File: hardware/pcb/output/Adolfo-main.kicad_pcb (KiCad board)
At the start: 2 copper layers, 96.2 x 110.5 mm, 156 parts, among them U1 Daisy Seed 3 / Seed2 DFM comp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, U10 OPA4197ID candidate, U11 OPA4197ID candidate, U12 SN74AHCT125 candidate, U13 SN74AHCT125 candidate, U2 AD7606C-18 candidate, U3 DAC8568B (gain 1, midscale re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, U4 MCP23017-E/SO candidate, U5 SN74LVC08A candidate, U6 SN74LVC08A candidate, U7 ADG5412FBRUZ candidate, U8 ADG5412FBRUZ candidate, U9 OPA4197ID candidate

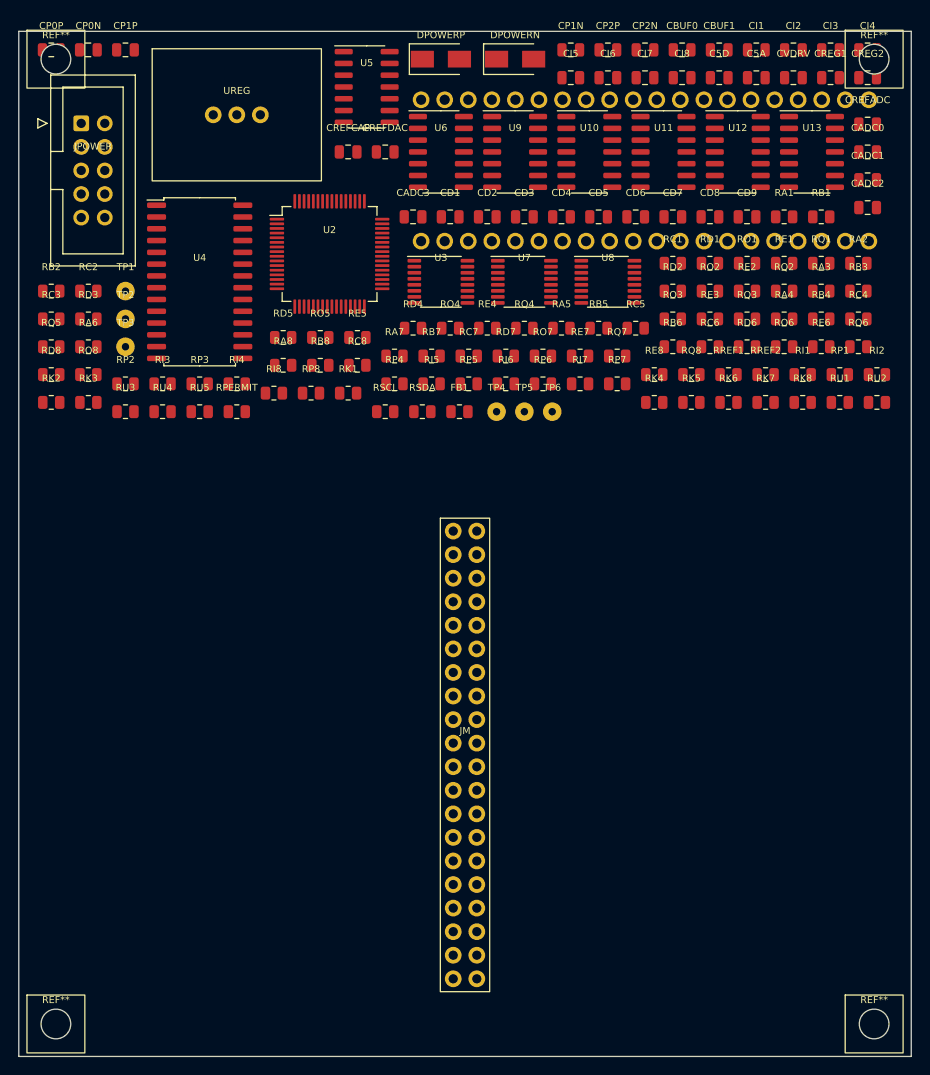
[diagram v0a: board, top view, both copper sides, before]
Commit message: fix(pcb): harden 20hp carrier and center panel display
Complete rev D schematics, routed boards and native KiCad checks.
Fix input normals, reset latch, fault resistor ratings and via placement.
Center the OLED module and window; update routing and mechanical exports.
Record supply sequencing, 5 V supervision and converter backend blockers.

Validation: 2027 CAD checks, zero ERC/DRC violations, host and SPICE tests.
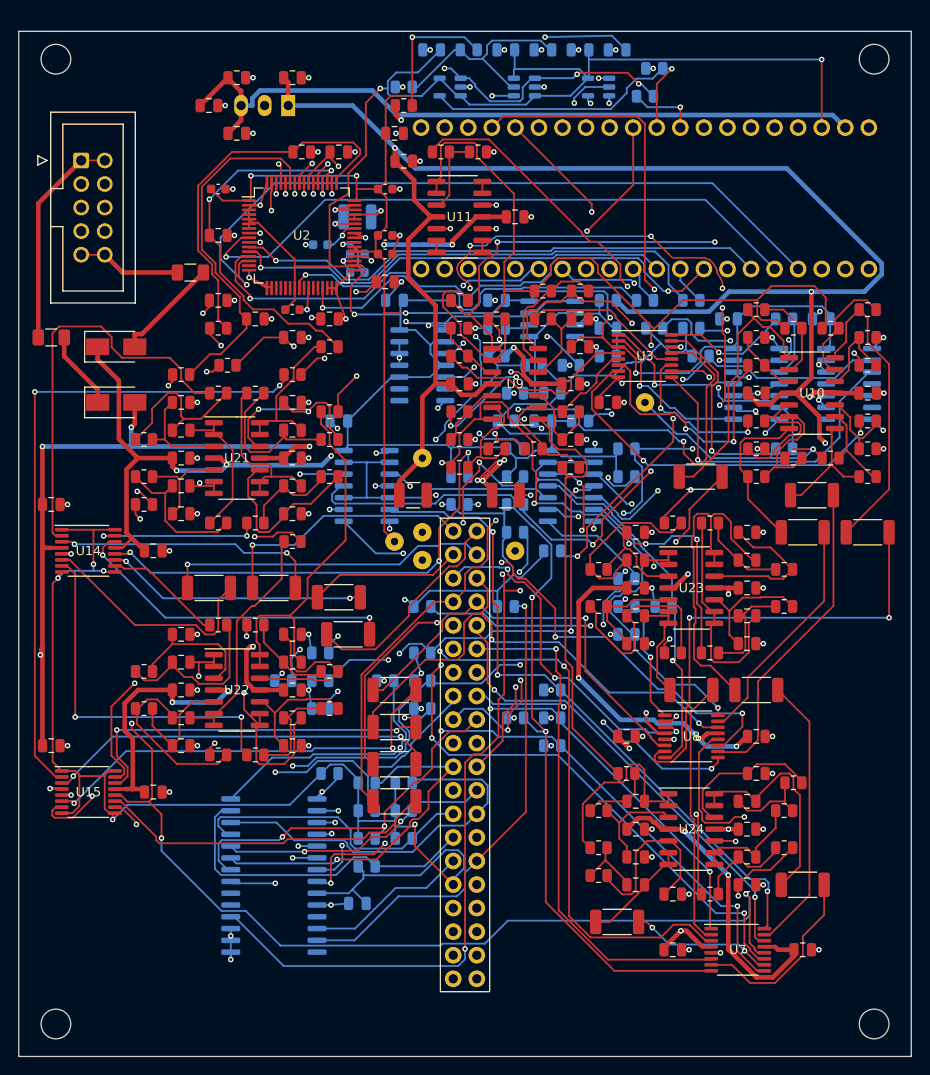
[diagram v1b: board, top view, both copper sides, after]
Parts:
- removed C5A: 10uF 10V, ADOLFO:c0805
- removed C5D: 47uF 10V, ADOLFO:c0805
- removed CP0N, CP0P, CP1N, CP1P, CP2N, CP2P: 100nF 50V, ADOLFO:c0805
- removed CREFADC, CREFDAC, CVDRV: 100nF, ADOLFO:c0805
- removed CREFCAP: 10uF low ESR, ADOLFO:c0805
- removed DPOWERN, DPOWERP: SS14, ADOLFO:sma
- removed JM: Panel link 2x20 candidate, ADOLFO:header40
- removed JPOWER: Eurorack IDC10 keyed, ADOLFO:idc10
- removed RPERMIT: 10k, ADOLFO:r0805
- removed RSCL, RSDA: 4.7k DNP, ADOLFO:r0805
- removed UREG: 5V >=1A module - selection OPEN, ADOLFO:power_module
- added C1: 100nF 50V, ADOLFO:c0805, F.Cu at (50.0, 47.0)
- added C10: 100nF, ADOLFO:c0603, B.Cu at (35.0, 32.0)
- added C11: 10uF 25V X7R low ESR, ADOLFO:c1210, B.Cu at (39.0, 29.0)
- added C12: 100nF, ADOLFO:c0805, F.Cu at (66.0, 49.0)
- added C13: 10nF, ADOLFO:c0805, B.Cu at (66.0, 41.0)
- added C14: 1nF, ADOLFO:c0805, B.Cu at (54.0, 41.0)
- added C15: 10nF, ADOLFO:c0805, B.Cu at (67.0, 11.0)
- added C16: 100nF 50V, ADOLFO:c0805, F.Cu at (17.0, 65.0)
- added C17: 100nF 50V, ADOLFO:c0805, F.Cu at (6.00, 60.0)
- added C18: 100nF 50V, ADOLFO:c0805, F.Cu at (17.0, 91.0)
- added C19: 100nF 50V, ADOLFO:c0805, F.Cu at (6.00, 86.0)
- added C2: 100nF 50V, ADOLFO:c0805, F.Cu at (62.0, 47.0)
- added C20: 820pF C0G 1%, ADOLFO:c0805, F.Cu at (20.0, 52.0)
- added C21: 680pF C0G 1%, ADOLFO:c0805, F.Cu at (20.0, 49.0)
- added C22: 1.8nF C0G 1%, ADOLFO:c0805, F.Cu at (20.0, 58.0)
- added C23: 270pF C0G 1%, ADOLFO:c0805, F.Cu at (20.0, 61.0)
- added C24: 820pF C0G 1%, ADOLFO:c0805, F.Cu at (32.0, 58.0)
- added C25: 680pF C0G 1%, ADOLFO:c0805, F.Cu at (32.0, 61.0)
- added C26: 1.8nF C0G 1%, ADOLFO:c0805, F.Cu at (32.0, 52.0)
- added C27: 270pF C0G 1%, ADOLFO:c0805, F.Cu at (32.0, 49.0)
- added C28: 820pF C0G 1%, ADOLFO:c0805, F.Cu at (20.0, 77.0)
- added C29: 680pF C0G 1%, ADOLFO:c0805, F.Cu at (20.0, 74.0)
- added C3: 100nF 50V, ADOLFO:c0805, F.Cu at (82.0, 48.0)
- added C30: 1.8nF C0G 1%, ADOLFO:c0805, F.Cu at (20.0, 83.0)
- added C31: 270pF C0G 1%, ADOLFO:c0805, F.Cu at (20.0, 86.0)
- added C32: 820pF C0G 1%, ADOLFO:c0805, F.Cu at (32.0, 83.0)
- added C33: 680pF C0G 1%, ADOLFO:c0805, F.Cu at (32.0, 86.0)
- added C34: 1.8nF C0G 1%, ADOLFO:c0805, F.Cu at (32.0, 77.0)
- added C35: 270pF C0G 1%, ADOLFO:c0805, F.Cu at (32.0, 74.0)
- added C36: 820pF C0G 1%, ADOLFO:c0805, F.Cu at (69.0, 66.0)
- added C37: 680pF C0G 1%, ADOLFO:c0805, F.Cu at (69.0, 63.0)
- added C38: 1.8nF C0G 1%, ADOLFO:c0805, F.Cu at (69.0, 72.0)
- added C39: 270pF C0G 1%, ADOLFO:c0805, F.Cu at (69.0, 75.0)
- added C4: 100nF 50V, ADOLFO:c0805, F.Cu at (94.0, 48.0)
- added C40: 820pF C0G 1%, ADOLFO:c0805, F.Cu at (81.0, 72.0)
- added C41: 680pF C0G 1%, ADOLFO:c0805, F.Cu at (81.0, 75.0)
- added C42: 1.8nF C0G 1%, ADOLFO:c0805, F.Cu at (81.0, 66.0)
- added C43: 270pF C0G 1%, ADOLFO:c0805, F.Cu at (81.0, 63.0)
- added C44: 820pF C0G 1%, ADOLFO:c0805, F.Cu at (69.0, 92.0)
- added C45: 680pF C0G 1%, ADOLFO:c0805, F.Cu at (69.0, 98.0)
- added C46: 1.8nF C0G 1%, ADOLFO:c0805, F.Cu at (69.0, 101.0)
- added C47: 270pF C0G 1%, ADOLFO:c0805, F.Cu at (73.0, 102.0)
- added C48: 820pF C0G 1%, ADOLFO:c0805, F.Cu at (81.0, 98.0)
- added C49: 680pF C0G 1%, ADOLFO:c0805, F.Cu at (81.0, 101.0)
- added C5: 100nF 50V, ADOLFO:c0805, F.Cu at (44.0, 23.0)
- added C50: 1.8nF C0G 1%, ADOLFO:c0805, F.Cu at (81.0, 92.0)
- added C51: 270pF C0G 1%, ADOLFO:c0805, F.Cu at (82.0, 89.0)
- added C52: 100nF 50V, ADOLFO:c0805, F.Cu at (20.0, 55.0)
- added C53: 100nF 50V, ADOLFO:c0805, F.Cu at (32.0, 55.0)
- added C54: 100nF 50V, ADOLFO:c0805, F.Cu at (20.0, 80.0)
- added C55: 100nF 50V, ADOLFO:c0805, F.Cu at (32.0, 80.0)
- added C56: 100nF 50V, ADOLFO:c0805, F.Cu at (69.0, 69.0)
- added C57: 100nF 50V, ADOLFO:c0805, F.Cu at (81.0, 69.0)
- added C58: 100nF 50V, ADOLFO:c0805, F.Cu at (69.0, 95.0)
- added C59: 100nF 50V, ADOLFO:c0805, F.Cu at (81.0, 95.0)
- added C6: 100nF 50V, ADOLFO:c0805, F.Cu at (56.0, 29.0)
- added C60: 22uF 25V X7R, ADOLFO:c1210, F.Cu at (45.0, 59.0)
- added C61: 22uF 25V X7R, ADOLFO:c1210, F.Cu at (55.0, 59.0)
- added C62: 100nF 50V, ADOLFO:c0805, F.Cu at (32.0, 14.0)
- added C63: 100nF, ADOLFO:c0805, F.Cu at (23.0, 17.0)
- added C7: 47uF 10V, ADOLFO:c0805, F.Cu at (26.0, 14.0)
- added C8: 10uF 10V, ADOLFO:c0805, F.Cu at (43.0, 20.0)
- added C9: 100nF, ADOLFO:c0603, F.Cu at (32.0, 39.0)
- added CMON5: 10nF, ADOLFO:c0805, B.Cu at (59.0, 11.0)
- added CSAFE16: 100nF, ADOLFO:c0805, B.Cu at (43.0, 38.0)
- added CSAFE17: 100nF, ADOLFO:c0805, B.Cu at (47.0, 11.0)
- added CSAFE18: 100nF, ADOLFO:c0805, B.Cu at (55.0, 11.0)
- added CSAFE19: 100nF, ADOLFO:c0805, B.Cu at (54.0, 38.0)
- added CSAFE20: 100nF, ADOLFO:c0805, B.Cu at (63.0, 11.0)
- added D1: SS14, ADOLFO:sma, F.Cu at (13.0, 43.0)
- added D2: SS14, ADOLFO:sma, F.Cu at (13.0, 49.0)
- added D3: BAT54WS, ADOLFO:sod323, B.Cu at (52.0, 47.0)
- added F1: Littelfuse 1206L075/24YR, ADOLFO:fuse1206, F.Cu at (21.0, 35.0)
- added F2: Littelfuse 1206L025/30YR, ADOLFO:fuse1206, F.Cu at (6.00, 42.0)
- added J13: Samtec TSW-120-07-G-D, ADOLFO:header40, F.Cu at (50.6, 87.0)
- added J16: Wurth 61201021621 IDC10, ADOLFO:idc10, F.Cu at (10.5, 28.0)
- added R1: 10k, ADOLFO:r0805, B.Cu at (62.0, 45.0)
- added R10: 11k 0.1%, ADOLFO:r0805, F.Cu at (16.0, 53.0)
- added R11: 11k 0.1%, ADOLFO:r0805, F.Cu at (24.0, 62.0)
- added R12: 11k 0.1%, ADOLFO:r0805, F.Cu at (16.0, 57.0)
- added R13: 11k 0.1%, ADOLFO:r0805, F.Cu at (28.0, 62.0)
- added R14: 11k 0.1%, ADOLFO:r0805, F.Cu at (36.0, 57.0)
- added R15: 11k 0.1%, ADOLFO:r0805, F.Cu at (28.0, 48.0)
- added R16: 11k 0.1%, ADOLFO:r0805, F.Cu at (36.0, 53.0)
- added R17: 11k 0.1%, ADOLFO:r0805, F.Cu at (24.0, 73.0)
- added R18: 11k 0.1%, ADOLFO:r0805, F.Cu at (16.0, 78.0)
- added R19: 11k 0.1%, ADOLFO:r0805, F.Cu at (24.0, 87.0)
- added R2: 2.2k, ADOLFO:r0805, B.Cu at (46.0, 71.0)
- added R20: 11k 0.1%, ADOLFO:r0805, F.Cu at (16.0, 82.0)
- added R21: 11k 0.1%, ADOLFO:r0805, F.Cu at (28.0, 87.0)
- added R22: 11k 0.1%, ADOLFO:r0805, F.Cu at (36.0, 82.0)
- added R23: 11k 0.1%, ADOLFO:r0805, F.Cu at (28.0, 73.0)
- added R24: 11k 0.1%, ADOLFO:r0805, F.Cu at (36.0, 78.0)
- added R25: 11k 0.1%, ADOLFO:r0805, F.Cu at (73.0, 62.0)
- added R26: 11k 0.1%, ADOLFO:r0805, F.Cu at (65.0, 67.0)
- added R27: 11k 0.1%, ADOLFO:r0805, F.Cu at (73.0, 76.0)
- added R28: 11k 0.1%, ADOLFO:r0805, F.Cu at (65.0, 71.0)
- added R29: 11k 0.1%, ADOLFO:r0805, F.Cu at (77.0, 76.0)
- added R3: 2.2k, ADOLFO:r0805, B.Cu at (55.0, 71.0)
- added R30: 11k 0.1%, ADOLFO:r0805, F.Cu at (85.0, 71.0)
- added R31: 11k 0.1%, ADOLFO:r0805, F.Cu at (77.0, 62.0)
- added R32: 11k 0.1%, ADOLFO:r0805, F.Cu at (85.0, 67.0)
- added R33: 11k 0.1%, ADOLFO:r0805, F.Cu at (68.0, 89.0)
- added R34: 11k 0.1%, ADOLFO:r0805, F.Cu at (65.0, 93.0)
- added R35: 11k 0.1%, ADOLFO:r0805, F.Cu at (65.0, 97.0)
- added R36: 11k 0.1%, ADOLFO:r0805, F.Cu at (65.0, 100.0)
- added R37: 11k 0.1%, ADOLFO:r0805, F.Cu at (77.0, 102.0)
- added R38: 11k 0.1%, ADOLFO:r0805, F.Cu at (85.0, 97.0)
- added R39: 11k 0.1%, ADOLFO:r0805, F.Cu at (85.0, 93.0)
- added R4: 0R, ADOLFO:r0805, B.Cu at (70.0, 16.0)
- added R40: 11k 0.1%, ADOLFO:r0805, F.Cu at (86.0, 90.0)
- added R41: 10k, ADOLFO:r0805, B.Cu at (68.0, 54.0)
- added R42: 33R, ADOLFO:r0805, B.Cu at (75.0, 38.0)
- added R43: 33R, ADOLFO:r0805, B.Cu at (70.0, 38.0)
- added R44: 33R, ADOLFO:r0805, B.Cu at (85.0, 40.0)
- added R45: 33R, ADOLFO:r0805, B.Cu at (85.0, 54.0)
- added R5: 10k, ADOLFO:r0805, B.Cu at (50.0, 57.0)
- added R6: 10k, ADOLFO:r0805, B.Cu at (71.0, 13.0)
- added R7: 109k 0.1%, ADOLFO:r0805, B.Cu at (51.0, 11.0)
- added R8: 10k 0.1%, ADOLFO:r0805, B.Cu at (44.0, 15.0)
- added R9: 11k 0.1%, ADOLFO:r0805, F.Cu at (24.0, 48.0)
- added RADCF1: 47R, ADOLFO:r0805, F.Cu at (24.0, 41.0)
- added RADCF2: 47R, ADOLFO:r0805, F.Cu at (36.0, 43.0)
- added RADCF3: 47R, ADOLFO:r0805, F.Cu at (32.0, 64.0)
- added RADCF4: 47R, ADOLFO:r0805, F.Cu at (36.0, 50.0)
- added RIC5: 1k, ADOLFO:r0805, F.Cu at (32.0, 46.0)
- added RIC6: 1k, ADOLFO:r0805, F.Cu at (20.0, 46.0)
- added RIC7: 1k, ADOLFO:r0805, F.Cu at (25.0, 45.0)
- added RIC8: 1k, ADOLFO:r0805, F.Cu at (16.0, 60.0)
- added RMONREF1: 10k 0.1%, ADOLFO:r0805, B.Cu at (60.0, 48.0)
- added RMONREF2: 10k 0.1%, ADOLFO:r0805, B.Cu at (56.0, 48.0)
- added RNMON1: 1M 0.1%, ADOLFO:r0805, B.Cu at (54.0, 44.0)
- added RNMON2: 137k 0.1%, ADOLFO:r0805, B.Cu at (58.0, 45.0)
- added RPMON1: 53.1k 0.1%, ADOLFO:r0805, B.Cu at (66.0, 38.0)
- added RPMON2: 10k 0.1%, ADOLFO:r0805, B.Cu at (66.0, 44.0)
- added U14: ADG5412FBRUZ, ADOLFO:tssop16, F.Cu at (10.0, 65.0)
- added U15: ADG5412FBRUZ, ADOLFO:tssop16, F.Cu at (10.0, 91.0)
- added U16: SN74HCS74DR, ADOLFO:soic14, B.Cu at (46.0, 45.0)
- added U17: TPS3828-33DBVR, ADOLFO:sot23_5, B.Cu at (49.0, 15.0)
- added U18: TPS3808G01DBVR, ADOLFO:sot23_6, B.Cu at (57.0, 15.0)
- added U19: LM393BDR, ADOLFO:soic8, B.Cu at (60.0, 40.0)
- added U20: SN74LVC1G08DBVR, ADOLFO:sot23_5, B.Cu at (65.0, 15.0)
- added U21: OPA4197ID, ADOLFO:soic14, F.Cu at (26.0, 55.0)
- added U22: OPA4197ID, ADOLFO:soic14, F.Cu at (26.0, 80.0)
- added U23: OPA4197ID, ADOLFO:soic14, F.Cu at (75.0, 69.0)
- added U24: OPA4197ID, ADOLFO:soic14, F.Cu at (75.0, 95.0)
- added U25: R-78E5.0-1.0, ADOLFO:recom, B.Cu at (29.0, 17.0)
- CADC0, CADC1, CADC2, CADC3: footprint ADOLFO:c0805 -> ADOLFO:c0603
- CBUF0, CBUF1, CD3, CD4, CD5, RE1, RE2, RE3, RE4, RE5, RE6, RE7, RE8, RK1, RK2, RK3, RK4, RK5, RK6, RK7, RK8, RP1, RP2, RP3, RP4, RP5, RP6, RP7, RP8, RQ1, RQ2, RQ3, RQ4, RQ5, RQ6, RQ7, RQ8, RU1, RU2, RU3, RU4, RU5: moved to B.Cu
- CI1, CI2, CI3, CI4: value 1nF EMI only - NOT full antialias -> 100pF C0G
- CI5, CI6, CI7, CI8: value 1nF EMI only - NOT full antialias -> 1nF C0G
- CREG1, CREG2: footprint ADOLFO:c0805 -> ADOLFO:c0603; moved to B.Cu
- FB1: value Ferrite 600R@100MHz candidate -> BLM21PG601SN1D
- RA1, RA2, RA3, RA4, RA5, RA6, RA7, RA8, RC1, RC2, RC3, RC4, RC5, RC6, RC7, RC8: value 10k 0.01% matched network TBD -> 10k 0.1%
- RB1, RB2, RB3, RB4, RB5, RB6, RB7, RB8, RD1, RD2, RD3, RD4, RD5, RD6, RD7, RD8: value 40k 0.01% matched network TBD -> 40k 0.1%
- RI1, RI2, RI3, RI4, RI5, RI6, RI7, RI8: value 1k input protection candidate -> 1k 1W 1%; footprint ADOLFO:r0805 -> ADOLFO:r2010
- RO1, RO2, RO3, RO4, RO5, RO6, RO7, RO8: value 100R 0.25W candidate -> 1k 1W 1%; footprint ADOLFO:r0805 -> ADOLFO:r2010
- RREF1, RREF2: value 10k 0.01% matched -> 10k 0.1%
- U1: value Daisy Seed 3 / Seed2 DFM compatibility review -> Daisy Seed 3
- U10, U11, U9: value OPA4197ID candidate -> OPA4197ID
- U12, U13: value SN74AHCT125 candidate -> SN74AHCT125DR; moved to B.Cu
- U2: value AD7606C-18 candidate -> AD7606C-18BSTZ
- U3: value DAC8568B (gain 1, midscale reset) candidate -> DAC8568BPW
- U4: value MCP23017-E/SO candidate -> MCP23017-E/SO; moved to B.Cu
- U5, U6: value SN74LVC08A candidate -> SN74LVC08ADR; moved to B.Cu
- U7, U8: value ADG5412FBRUZ candidate -> ADG5412FBRUZ
- moved RD8 88.3 mm to (94.0, 39.0)
- moved RO8 85.7 mm to (94.0, 63.0)
- moved CD6 81.0 mm to (87.0, 108.0)
- moved CD7 79.0 mm to (73.0, 108.0)
- moved CD3 76.2 mm to (39.0, 103.0), turned to 180 degrees
- moved U7 75.6 mm to (80.0, 108.0)
- moved RA6 72.4 mm to (82.0, 51.0)
- moved RO4 71.0 mm to (87.0, 101.0)
- moved RQ1 70.3 mm to (35.0, 79.0), turned to 180 degrees
- moved CADC0 70.1 mm to (24.0, 26.0)
- moved RK7 65.9 mm to (40.0, 99.0), turned to 180 degrees
- moved RO3 65.3 mm to (67.0, 105.0)
- moved CI2 65.1 mm to (24.0, 31.0)
- moved RK8 64.8 mm to (36.0, 89.0), turned to 180 degrees
- moved U4 64.5 mm to (30.0, 100.0), turned to 180 degrees
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- renumbered REF** to H1, REF** to H2, REF** to H3, REF** to H4
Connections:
- RI1 pad 2: ADC_IN1 -> INPUT_LIMIT1
- RI2 pad 2: ADC_IN2 -> INPUT_LIMIT2
- RI3 pad 2: ADC_IN3 -> INPUT_LIMIT3
- RI4 pad 2: ADC_IN4 -> INPUT_LIMIT4
- RI5 pad 2: ADC_IN5 -> INPUT_LIMIT5
- RI6 pad 2: ADC_IN6 -> INPUT_LIMIT6
- RI7 pad 2: ADC_IN7 -> INPUT_LIMIT7
- RI8 pad 2: ADC_IN8 -> INPUT_LIMIT8
- RO1 pad 1: AMP1 -> OUT1F2_OUT
- RO2 pad 1: AMP2 -> OUT2F2_OUT
- RO3 pad 1: AMP3 -> OUT3F2_OUT
- RO4 pad 1: AMP4 -> OUT4F2_OUT
- U1 pad 16: (no net) -> unconnected-(U1-AUDIO_IN_L-Pad16)
- U1 pad 17: (no net) -> unconnected-(U1-AUDIO_IN_R-Pad17)
- U1 pad 18: (no net) -> unconnected-(U1-AUDIO_OUT_L-Pad18)
- U1 pad 19: (no net) -> unconnected-(U1-AUDIO_OUT_R-Pad19)
- U1 pad 21: (no net) -> unconnected-(U1-+3V3A-Pad21)
- U1 pad 31: (no net) -> WATCHDOG
- U1 pad 32: (no net) -> FAULT_N
- U1 pad 33: (no net) -> OLED_RESET
- U1 pad 34: (no net) -> unconnected-(U1-D27-Pad34)
- U1 pad 35: (no net) -> unconnected-(U1-D28-Pad35)
- U1 pad 36: (no net) -> unconnected-(U1-D29-Pad36)
- U1 pad 37: (no net) -> unconnected-(U1-D30-Pad37)
- U12 pad 3: DAC_SCK_5V -> DAC_SCK_BUFFER
- U12 pad 6: DAC_MOSI_5V -> DAC_MOSI_BUFFER
- U13 pad 11: (no net) -> unconnected-(U13-Pad11)
- U13 pad 6: (no net) -> unconnected-(U13-Pad6)
- U13 pad 8: (no net) -> unconnected-(U13-Pad8)
- U2 pad 12: ADC_SCK -> ADC_SCK_TERM
- U2 pad 15: (no net) -> unconnected-(U2-FRSTDATA-Pad15)
- U2 pad 19: (no net) -> unconnected-(U2-DB3-Pad19)
- U2 pad 20: (no net) -> unconnected-(U2-DB4-Pad20)
- U2 pad 21: (no net) -> unconnected-(U2-DB5-Pad21)
- U2 pad 22: (no net) -> unconnected-(U2-DB6-Pad22)
- U2 pad 25: (no net) -> unconnected-(U2-DB10_DOUTB-Pad25)
- U2 pad 27: (no net) -> unconnected-(U2-DB11_DOUTC-Pad27)
- U2 pad 28: (no net) -> unconnected-(U2-DB12_DOUTD-Pad28)
- U2 pad 29: ADC_MOSI -> ADC_MOSI_TERM
- U4 pad 1: REQ5 -> KEY4
- U4 pad 10: (no net) -> GND
- U4 pad 11: GND -> unconnected-(U4-NC-Pad11)
- U4 pad 12: GND -> I2C_SCL
- U4 pad 13: GND -> I2C_SDA
- U4 pad 14: IO_RESET -> unconnected-(U4-NC-Pad14)
- U4 pad 15: (no net) -> GND
- U4 pad 16: (no net) -> GND
- U4 pad 17: ENC1_CLICK -> GND
- U4 pad 18: ENC2_CLICK -> IO_RESET
- U4 pad 19: ENC3_CLICK -> unconnected-(U4-INTB-Pad19)
- U4 pad 2: REQ6 -> REQ1
- U4 pad 20: ENC4_CLICK -> unconnected-(U4-INTA-Pad20)
- U4 pad 21: KEY1 -> ENC1_CLICK
- U4 pad 22: KEY2 -> ENC2_CLICK
- U4 pad 23: KEY3 -> ENC3_CLICK
- U4 pad 24: KEY4 -> ENC4_CLICK
- U4 pad 25: REQ1 -> KEY1
- U4 pad 26: REQ2 -> KEY2
- U4 pad 27: REQ3 -> KEY3
- U4 pad 28: REQ4 -> REQ8
- U4 pad 3: REQ7 -> REQ2
- U4 pad 4: REQ8 -> REQ3
- U4 pad 5: +3V3 -> REQ4
- U4 pad 6: GND -> REQ5
- U4 pad 7: (no net) -> REQ6
- U4 pad 8: I2C_SCL -> REQ7
- U4 pad 9: I2C_SDA -> +3V3
- U5 pad 10: OUTPUT_PERMIT -> SAFE_PERMIT
- U5 pad 13: OUTPUT_PERMIT -> SAFE_PERMIT
- U5 pad 2: OUTPUT_PERMIT -> SAFE_PERMIT
- U5 pad 5: OUTPUT_PERMIT -> SAFE_PERMIT
- U6 pad 10: OUTPUT_PERMIT -> SAFE_PERMIT
- U6 pad 13: OUTPUT_PERMIT -> SAFE_PERMIT
- U6 pad 2: OUTPUT_PERMIT -> SAFE_PERMIT
- U6 pad 5: OUTPUT_PERMIT -> SAFE_PERMIT
- U7 pad 12: FAULT1 -> SAFE_CLEAR_N
- U8 pad 12: FAULT2 -> SAFE_CLEAR_N
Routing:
- net +3V3: track 0.00 -> 456.5 mm, vias 0 -> 11
- net +12VA: track 0.00 -> 440.1 mm, vias 0 -> 14
- net -12VA: track 0.00 -> 428.3 mm, vias 0 -> 28
- net SAFE_CLEAR_N: track 0.00 -> 287.5 mm, vias 0 -> 12
- net GND: track 0.00 -> 188.9 mm, vias 0 -> 132
- net +5A: track 0.00 -> 164.9 mm, vias 0 -> 6
- net IO_RESET: track 0.00 -> 137.9 mm, vias 0 -> 5
- net REF_BUF: track 0.00 -> 135.2 mm, vias 0 -> 4
- net +5D: track 0.00 -> 133.7 mm, vias 0 -> 1
- net I2C_SCL: track 0.00 -> 108.5 mm, vias 0 -> 1
- net ENC2_A: track 0.00 -> 107.6 mm, vias 0 -> 4
- net SAFE_PERMIT: track 0.00 -> 107.5 mm, vias 0 -> 2
- net OLED_RESET: track 0.00 -> 107.2 mm, vias 0 -> 2
- net ENC3_B: track 0.00 -> 103.5 mm, vias 0 -> 1
- net SW_ON4: track 0.00 -> 93.2 mm, vias 0 -> 2
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- added copper zone on In1.Cu, net GND
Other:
- copper layers 2 -> 4
- rule pad_to_mask_clearance: 0.0 -> 0
